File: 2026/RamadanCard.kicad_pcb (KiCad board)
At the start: 2 copper layers, 98.8 x 68 mm, 26 parts, among them J1 SK-3296S-01-L1, U1 ATtiny44A-M, U2 L78L05_SOT89

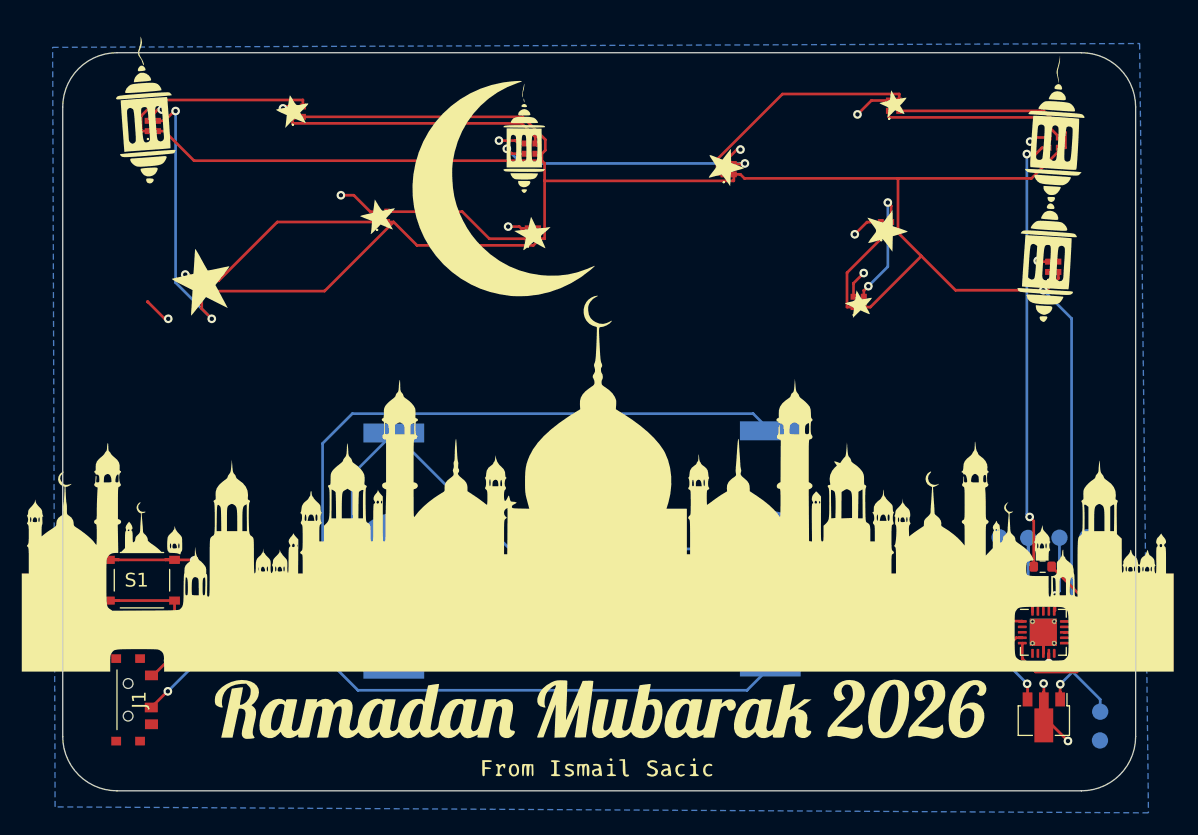
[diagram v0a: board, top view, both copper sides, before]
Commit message: Add new netlist file for 2026 production with detailed VIA and connection specifications
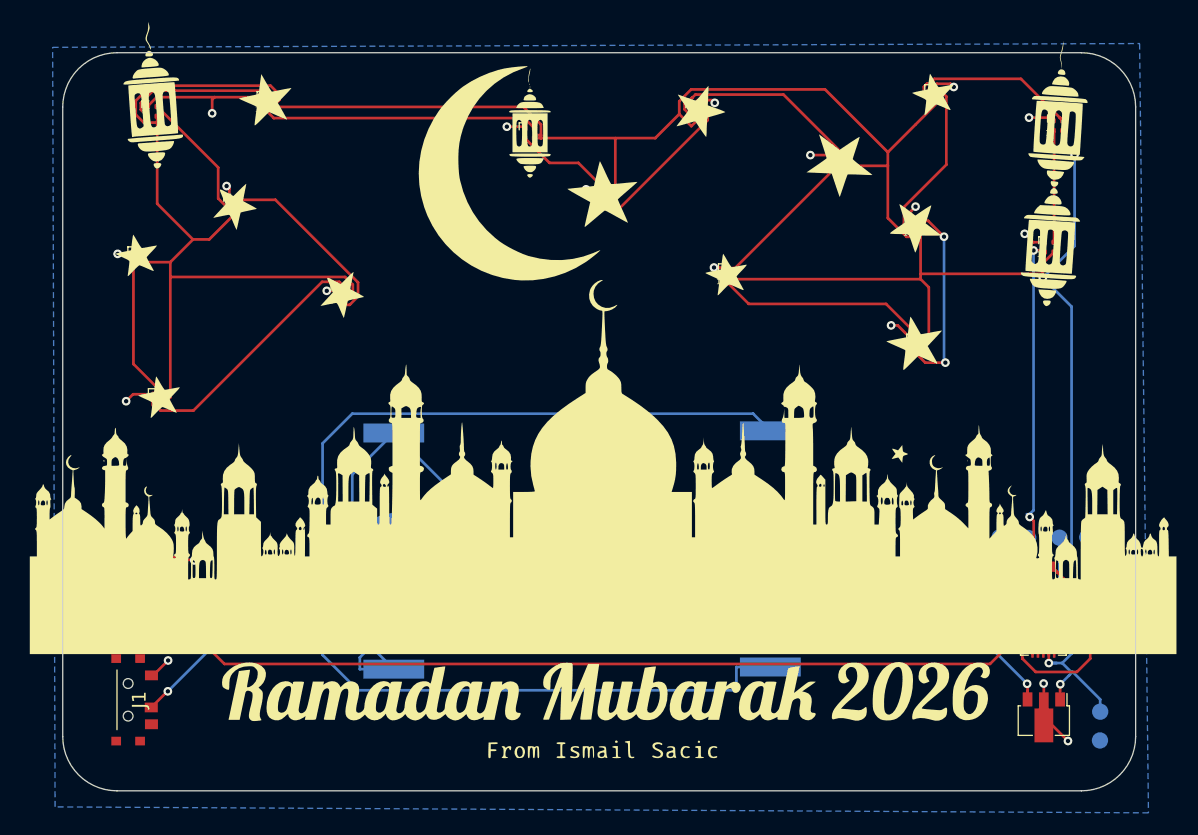
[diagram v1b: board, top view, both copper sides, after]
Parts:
- removed the G*** at (122.5, 103.5)
- added D10: SK6805, LED_SMD:LED_SK6812_EC15_1.5x1.5mm, F.Cu at (116.2, 78.0)
- added D11: SK6805, LED_SMD:LED_SK6812_EC15_1.5x1.5mm, F.Cu at (92.1, 75.1)
- added D12: SK6805, LED_SMD:LED_SK6812_EC15_1.5x1.5mm, F.Cu at (81.5, 76.0)
- added D13: SK6805, LED_SMD:LED_SK6812_EC15_1.5x1.5mm, F.Cu at (89.0, 84.5)
- added G***: LOGO, Graphics:Mosque2026-02-10, F.Cu at (123.0, 102.0)
- D1, D14, D15, D16, D2, D3, D4, D5, D6, D7, D8, D9: footprint Library:SK6805EC15 -> LED_SMD:LED_SK6812_EC15_1.5x1.5mm
- moved D16 84.3 mm to (80.2, 89.4)
- moved D15 65.1 mm to (82.0, 102.5)
- moved D5 60.9 mm to (151.9, 97.4)
- moved D7 59.4 mm to (144.8, 80.5)
- moved D6 54.8 mm to (134.6, 91.0)
- moved D14 50.5 mm to (98.9, 92.7)
- moved D4 36.2 mm to (151.8, 86.5)
- moved D8 30.5 mm to (131.6, 76.0)
- moved D3 20.2 mm to (153.6, 74.5)
- moved D2 15.2 mm to (164.9, 77.3)
- moved D1 9.63 mm to (164.1, 88.5)
- moved D9 7.31 mm to (123.0, 84.0)
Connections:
- D15 pad 1: Net-(D13-DOUT) -> Net-(D14-DOUT)
- D15 pad 3: Net-(D14-DOUT) -> Net-(D15-DOUT)
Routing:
- net Net-(D10-DOUT): track 0.00 -> 25.9 mm
- net +6V: track 258.9 -> 276.5 mm, vias 3 -> 4
- net Net-(D11-DOUT): track 0.00 -> 14.3 mm
- net Net-(D15-DOUT): track 0.00 -> 13.3 mm
- net Net-(D12-DOUT): track 0.00 -> 12.2 mm
- net Net-(D6-DOUT): track 25.4 -> 13.5 mm, vias 2 -> 0
- net Net-(D14-DOUT): track 11.5 -> 23.1 mm, vias 2 -> 0
- net Net-(D3-DOUT): track 25.4 -> 15.0 mm, vias 2 -> 0
- net Net-(D10-DIN): track 0.00 -> 9.86 mm
- net Net-(D13-DOUT): track 8.78 -> 17.9 mm
- net Net-(D1-DIN): track 40.5 -> 31.8 mm
- net GND: track 52.5 -> 60.6 mm, vias 17 -> 19
- net Net-(D1-DOUT): track 17.1 -> 10.3 mm
- net Net-(D4-DOUT): track 24.6 -> 18.4 mm, vias 0 -> 2
- net Net-(D2-DOUT): track 21.9 -> 16.8 mm
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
